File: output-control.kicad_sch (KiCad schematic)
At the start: 57 parts, among them U16 ADS7828, U17 TCA9534PWR, U18 ADS7828

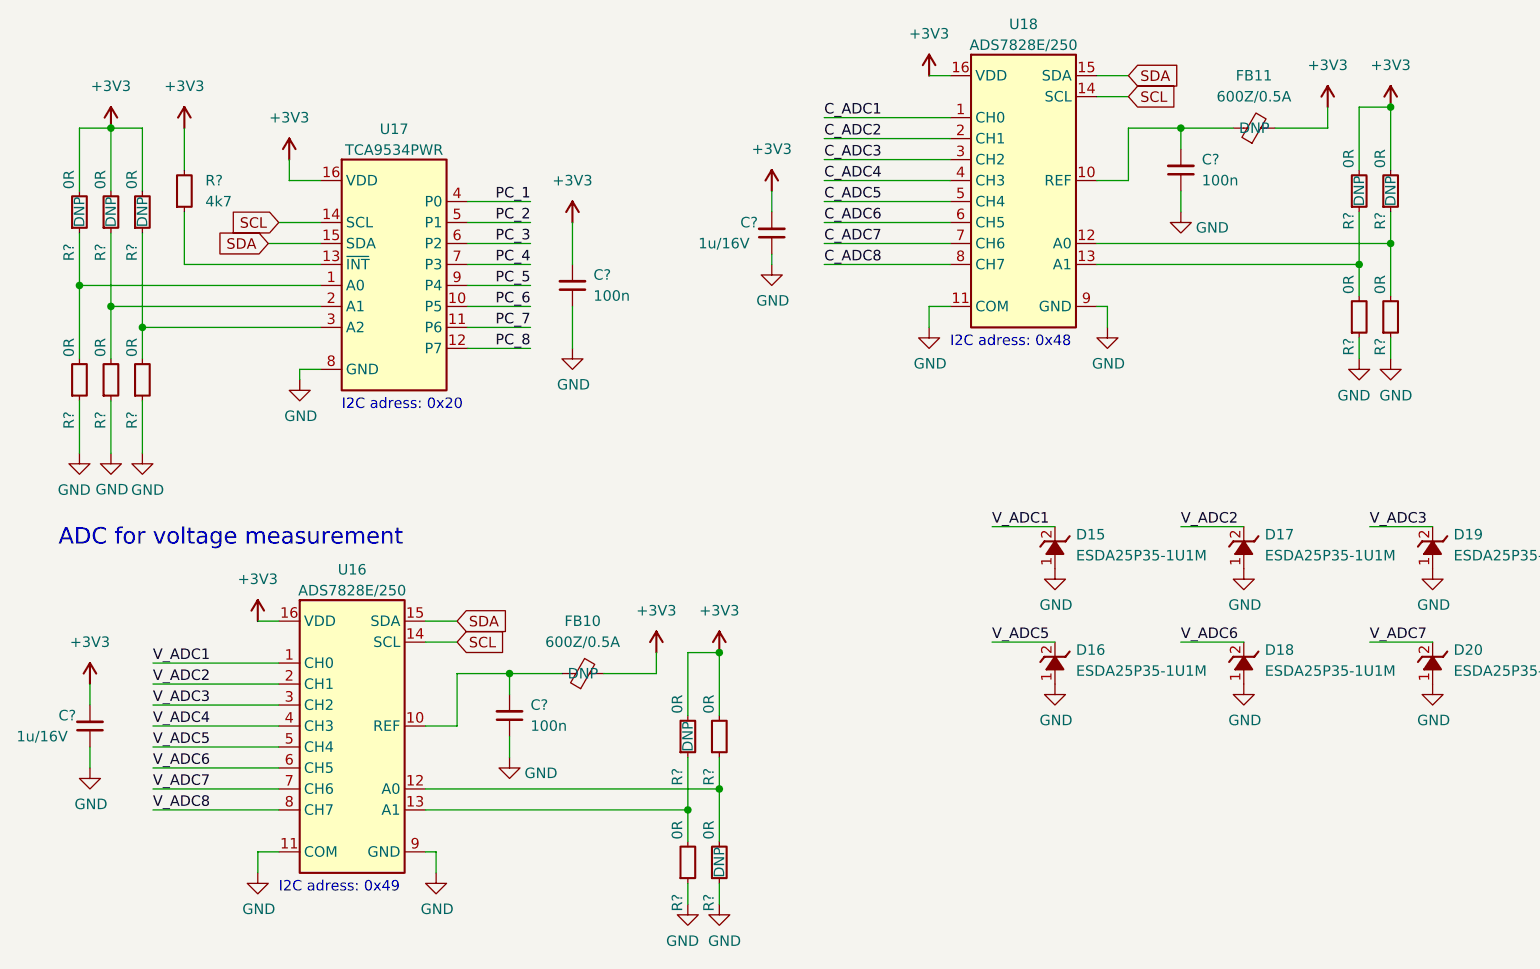
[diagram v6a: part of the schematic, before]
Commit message: Standarize debug signal schematic
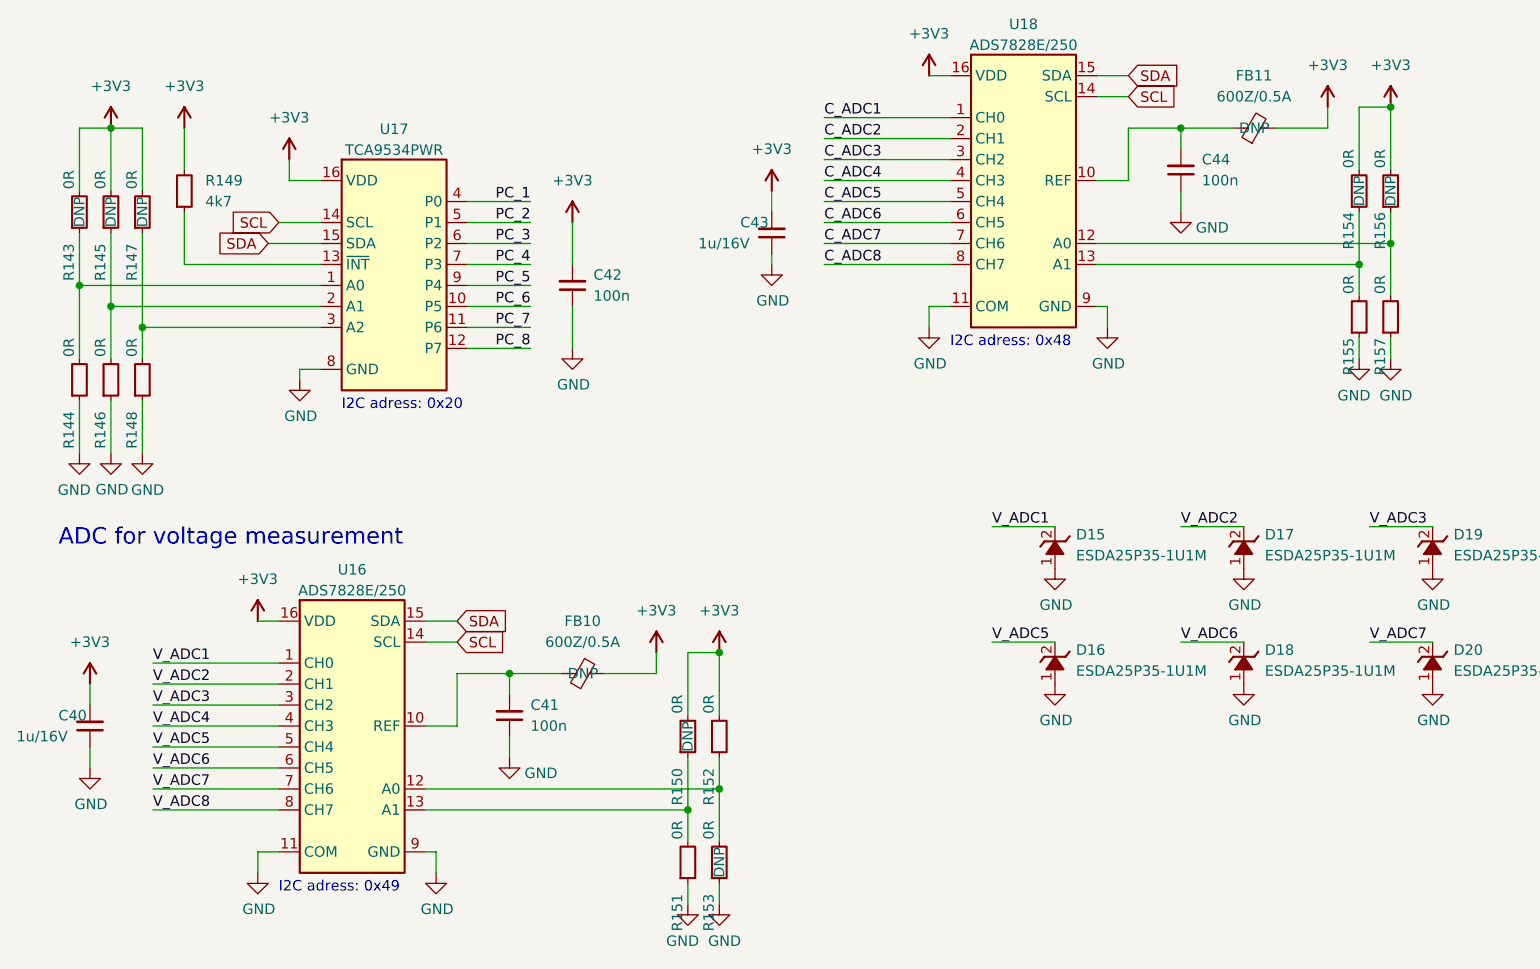
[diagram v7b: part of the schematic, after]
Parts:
- gave numbers to parts that had none: 20
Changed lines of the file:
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@@
   (symbol (lib_name "C_100n_0402_1") (lib_id "antmicroCapacitors0402:C_100n_0402") (at 69.85 161.29 90) (unit 1)
     (in_bom yes) (on_board yes) (fields_autoplaced)
-    (property "Reference" "C?" (id 0) (at 72.39 157.4735 90)
+    (property "Reference" "C41" (id 0) (at 72.39 157.4735 90)
       (effects (font (size 1.27 1.27) (thickness 0.15)) (justify right))
     )
@@
   (symbol (lib_name "R_0R_0402_1") (lib_id "antmicroResistors0402:R_0R_0402") (at 95.25 179.07 90) (unit 1)
     (in_bom yes) (on_board yes)
-    (property "Reference" "R?" (id 0) (at 93.98 180.34 0)
+    (property "Reference" "R153" (id 0) (at 93.98 180.34 0)
       (effects (font (size 1.27 1.27) (thickness 0.15)) (justify right))
     )
@@
   (symbol (lib_name "R_0R_0402_1") (lib_id "antmicroResistors0402:R_0R_0402") (at 17.78 120.65 90) (unit 1)
     (in_bom yes) (on_board yes)
-    (property "Reference" "R?" (id 0) (at 16.51 121.92 0)
+    (property "Reference" "R144" (id 0) (at 16.51 121.92 0)
       (effects (font (size 1.27 1.27) (thickness 0.15)) (justify right))
     )
@@
   (symbol (lib_name "R_0R_0402_2") (lib_id "antmicroResistors0402:R_0R_0402") (at 176.53 97.79 90) (unit 1)
     (in_bom yes) (on_board yes)
-    (property "Reference" "R?" (id 0) (at 175.26 97.79 0)
+    (property "Reference" "R156" (id 0) (at 175.26 97.79 0)
       (effects (font (size 1.27 1.27) (thickness 0.15)) (justify right))
     )
@@
   (symbol (lib_name "R_0R_0402_1") (lib_id "antmicroResistors0402:R_0R_0402") (at 91.44 163.83 90) (unit 1)
     (in_bom yes) (on_board yes)
-    (property "Reference" "R?" (id 0) (at 90.17 165.1 0)
+    (property "Reference" "R150" (id 0) (at 90.17 165.1 0)
       (effects (font (size 1.27 1.27) (thickness 0.15)) (justify right))
     )
@@
   (symbol (lib_name "R_0R_0402_1") (lib_id "antmicroResistors0402:R_0R_0402") (at 21.59 120.65 90) (unit 1)
     (in_bom yes) (on_board yes)
-    (property "Reference" "R?" (id 0) (at 20.32 121.92 0)
+    (property "Reference" "R146" (id 0) (at 20.32 121.92 0)
       (effects (font (size 1.27 1.27) (thickness 0.15)) (justify right))
     )
@@
   (symbol (lib_name "C_100n_0402_1") (lib_id "antmicroCapacitors0402:C_100n_0402") (at 151.13 95.25 90) (unit 1)
     (in_bom yes) (on_board yes) (fields_autoplaced)
-    (property "Reference" "C?" (id 0) (at 153.67 91.4335 90)
+    (property "Reference" "C44" (id 0) (at 153.67 91.4335 90)
       (effects (font (size 1.27 1.27) (thickness 0.15)) (justify right))
     )
@@
   (symbol (lib_name "R_0R_0402_2") (lib_id "antmicroResistors0402:R_0R_0402") (at 172.72 113.03 90) (unit 1)
     (in_bom yes) (on_board yes)
-    (property "Reference" "R?" (id 0) (at 171.45 113.03 0)
+    (property "Reference" "R155" (id 0) (at 171.45 113.03 0)
       (effects (font (size 1.27 1.27) (thickness 0.15)) (justify right))
     )
@@
   (symbol (lib_name "R_0R_0402_1") (lib_id "antmicroResistors0402:R_0R_0402") (at 25.4 100.33 90) (unit 1)
     (in_bom yes) (on_board yes)
-    (property "Reference" "R?" (id 0) (at 24.13 101.6 0)
+    (property "Reference" "R147" (id 0) (at 24.13 101.6 0)
       (effects (font (size 1.27 1.27) (thickness 0.15)) (justify right))
     )
@@
   (symbol (lib_name "R_0R_0402_1") (lib_id "antmicroResistors0402:R_0R_0402") (at 25.4 120.65 90) (unit 1)
     (in_bom yes) (on_board yes)
-    (property "Reference" "R?" (id 0) (at 24.13 121.92 0)
+    (property "Reference" "R148" (id 0) (at 24.13 121.92 0)
       (effects (font (size 1.27 1.27) (thickness 0.15)) (justify right))
     )
@@
   (symbol (lib_name "R_0R_0402_1") (lib_id "antmicroResistors0402:R_0R_0402") (at 21.59 100.33 90) (unit 1)
     (in_bom yes) (on_board yes)
-    (property "Reference" "R?" (id 0) (at 20.32 101.6 0)
+    (property "Reference" "R145" (id 0) (at 20.32 101.6 0)
       (effects (font (size 1.27 1.27) (thickness 0.15)) (justify right))
     )
@@
   (symbol (lib_name "R_0R_0402_2") (lib_id "antmicroResistors0402:R_0R_0402") (at 172.72 97.79 90) (unit 1)
     (in_bom yes) (on_board yes)
-    (property "Reference" "R?" (id 0) (at 171.45 97.79 0)
+    (property "Reference" "R154" (id 0) (at 171.45 97.79 0)
       (effects (font (size 1.27 1.27) (thickness 0.15)) (justify right))
     )
@@
   (symbol (lib_name "R_0R_0402_1") (lib_id "antmicroResistors0402:R_0R_0402") (at 95.25 163.83 90) (unit 1)
     (in_bom yes) (on_board yes)
-    (property "Reference" "R?" (id 0) (at 93.98 165.1 0)
+    (property "Reference" "R152" (id 0) (at 93.98 165.1 0)
       (effects (font (size 1.27 1.27) (thickness 0.15)) (justify right))
     )
@@
   (symbol (lib_name "C_100n_0402_1") (lib_id "antmicroCapacitors0402:C_100n_0402") (at 77.47 109.22 90) (unit 1)
     (in_bom yes) (on_board yes) (fields_autoplaced)
-    (property "Reference" "C?" (id 0) (at 80.01 105.4035 90)
+    (property "Reference" "C42" (id 0) (at 80.01 105.4035 90)
       (effects (font (size 1.27 1.27) (thickness 0.15)) (justify right))
     )
@@
   (symbol (lib_id "antmicroCapacitors0402:C_1u_16V_0402") (at 19.05 162.56 90) (unit 1)
     (in_bom yes) (on_board yes)
-    (property "Reference" "C?" (id 0) (at 15.24 158.75 90)
+    (property "Reference" "C40" (id 0) (at 15.24 158.75 90)
       (effects (font (size 1.27 1.27) (thickness 0.15)) (justify right))
     )
@@
   (symbol (lib_name "R_0R_0402_1") (lib_id "antmicroResistors0402:R_0R_0402") (at 91.44 179.07 90) (unit 1)
     (in_bom yes) (on_board yes)
-    (property "Reference" "R?" (id 0) (at 90.17 180.34 0)
+    (property "Reference" "R151" (id 0) (at 90.17 180.34 0)
       (effects (font (size 1.27 1.27) (thickness 0.15)) (justify right))
     )
@@
   (symbol (lib_name "R_0R_0402_2") (lib_id "antmicroResistors0402:R_0R_0402") (at 176.53 113.03 90) (unit 1)
     (in_bom yes) (on_board yes)
-    (property "Reference" "R?" (id 0) (at 175.26 113.03 0)
+    (property "Reference" "R157" (id 0) (at 175.26 113.03 0)
       (effects (font (size 1.27 1.27) (thickness 0.15)) (justify right))
     )
@@
   (symbol (lib_name "R_4k7_0402_1") (lib_id "antmicroResistors0402:R_4k7_0402") (at 30.48 97.79 90) (unit 1)
     (in_bom yes) (on_board yes) (fields_autoplaced)
-    (property "Reference" "R?" (id 0) (at 33.02 93.9799 90)
+    (property "Reference" "R149" (id 0) (at 33.02 93.9799 90)
       (effects (font (size 1.27 1.27) (thickness 0.15)) (justify right))
     )
@@
   (symbol (lib_name "R_0R_0402_1") (lib_id "antmicroResistors0402:R_0R_0402") (at 17.78 100.33 90) (unit 1)
     (in_bom yes) (on_board yes)
-    (property "Reference" "R?" (id 0) (at 16.51 101.6 0)
+    (property "Reference" "R143" (id 0) (at 16.51 101.6 0)
       (effects (font (size 1.27 1.27) (thickness 0.15)) (justify right))
     )
@@
   (symbol (lib_id "antmicroCapacitors0402:C_1u_16V_0402") (at 101.6 102.87 90) (unit 1)
     (in_bom yes) (on_board yes)
-    (property "Reference" "C?" (id 0) (at 97.79 99.06 90)
-      (effects (font (size 1.27 1.27) (thickness 0.15)) (justify right))
-    )
+    (property "Reference" "C43" (id 0) (at 97.79 99.06 90)
+      (effects (font (size 1.27 1.27) (thickness 0.15)) (justify right))
+    )
